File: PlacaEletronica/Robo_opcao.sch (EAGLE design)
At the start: 100 parts, among them IC1 7805DT, IC2 7805DT, J1 F-1X06-SIP-100-40, J2 S2B-PH-K-S(LF)(SN), J3 ZX62-B-5PA, Q1 SMD-TRANSISTORS-NPN-25V-500MW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, Q2 SMD-TRANSISTORS-NPN-25V-500MW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, Q4 SFH_3716, U1 ESP32-WROOM-32D, U2 AMS1117-3.3, U3 INTERFACE-CP2102-GMR(QFN28)QF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

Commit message: PlacaPrincipal_AlteracoesResistoresCapacitoresPinhead
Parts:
- C7: device rcl:C-EUC0402 -> Perfect_0402:CAP_0402
- R1, R44, R51, R52, R54, R55, R56, R57, R58: device resistors:R-EU_ -> Perfect_0402:RES_0402
- R53: device rcl:R-EU_R0603 -> Perfect_0402:RES_0402

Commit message: Biblioteca Waveform
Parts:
- removed U$2: TSOP4838, tsop-1:TSOP4838
- added Q5: TSOP4838, tsop:TSOP4838
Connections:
- net GND: now also Q5.GND; no longer U$2.GND
- net VDD33: now also Q5.V+; no longer U$2.V+
- net VP_SENSOR_IR: now also Q5.OUT; no longer U$2.OUT
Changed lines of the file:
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@@
 <setting verticaltext="up"/>
 </settings>
-<grid distance="50" unitdist="mil" unit="mil" style="lines" multiple="1" display="yes" altdistance="0.01" altunitdist="inch" altunit="inch"/>
+<grid distance="0.1" unitdist="inch" unit="inch" style="lines" multiple="1" display="no" altdistance="0.01" altunitdist="inch" altunit="inch"/>
 <layers>
 <layer number="1" name="Top" color="4" fill="1" visible="no" active="no"/>
@@
 <part name="C17" library="Perfect_0402" deviceset="CPOL_0402" device="" value="10uF"/>
 <part name="C18" library="Perfect_0402" deviceset="CPOL_0402" device="" value="20uF"/>
-<part name="U$2" library="tsop-1" deviceset="TSOP4838" device=""/>
+<part name="Q5" library="tsop" deviceset="TSOP4838" device=""/>
 </parts>
 <sheets>
@@
 <attribute name="VALUE" x="-164.211" y="203.454" size="1.778" layer="96" rot="R270"/>
 </instance>
-<instance part="U$2" gate="G$1" x="541.02" y="87.63" smashed="yes" rot="R270">
+<instance part="Q5" gate="G$1" x="541.02" y="87.63" smashed="yes" rot="R270">
 <attribute name="VALUE" x="549.402" y="93.472" size="1.778" layer="96" rot="R270"/>
 </instance>
@@
 <wire x1="535.94" y1="74.93" x2="532.13" y2="74.93" width="0.1524" layer="91"/>
 <label x="532.13" y="74.93" size="1.778" layer="95" rot="R180"/>
-<pinref part="U$2" gate="G$1" pin="GND"/>
+<pinref part="Q5" gate="G$1" pin="GND"/>
 <junction x="535.94" y="80.01"/>
 </segment>
@@
 <wire x1="546.1" y1="74.93" x2="549.91" y2="74.93" width="0.1524" layer="91"/>
 <label x="549.91" y="73.66" size="1.778" layer="95"/>
-<pinref part="U$2" gate="G$1" pin="V+"/>
+<pinref part="Q5" gate="G$1" pin="V+"/>
 <junction x="546.1" y="80.01"/>
 </segment>
@@
 <wire x1="541.02" y1="81.28" x2="541.02" y2="80.01" width="0.1524" layer="91"/>
 <label x="541.02" y="71.12" size="1.778" layer="95" rot="R180"/>
-<pinref part="U$2" gate="G$1" pin="OUT"/>
+<pinref part="Q5" gate="G$1" pin="OUT"/>
 <wire x1="541.02" y1="80.01" x2="541.02" y2="74.93" width="0.1524" layer="91"/>
 <junction x="541.02" y="80.01"/>

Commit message: [MODIFIED] Troca de pinagem na placa principal
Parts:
- removed J1: F-1X06-SIP-100-40, con-headers-jp(1):F-1X06-SIP-100-40
- removed JP10: F-1X10-SIP-100-40, con-headers-jp(1):F-1X10-SIP-100-40
- removed JP11, JP8: F-1X08-SIP-100-40, con-headers-jp(1):F-1X08-SIP-100-40
- removed JP2: F-1X05-SIP-100-40, con-headers-jp(1):F-1X05-SIP-100-40
- added J4: F-1X06-SIP-100-40, con-headers-jp(1):F-1X06-SIP-100-40
- added JP3, JP9: F-1X08-SIP-100-40, con-headers-jp(1):F-1X08-SIP-100-40
- added JP6: F-1X10-SIP-100-40, con-headers-jp(1):F-1X10-SIP-100-40
- added JP7: F-1X05-SIP-100-40, con-headers-jp(1):F-1X05-SIP-100-40
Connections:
- removed net 10(5V): U1.IO12, V3/2.B
- removed net 11(5V): U1.IO5, V3/3.B
- removed net 12(5V): U1.SHD/SD2, V3/4.B
- removed net 13(5V): U1.IO4, V4/1.B
- removed net 1_S: J1.1, U1.IO34
- removed net 2_S: J1.2, U1.IO35
- removed net 3_S: J1.3, U1.IO32
- removed net 4_S: J1.4, U1.IO33
- removed net 5_S: J1.5, U1.IO25
- removed net 6_S: J1.6, U1.IO26
- removed net 7_S: JP2.2, U1.IO27
- removed net 8_S: JP2.3, U1.IO15
- removed net 9(5V): U1.IO13, V3/1.B
- removed net N$29: JP8.1
- removed net N$48: JP10.8
- removed net PORT_10~5V: D11.A, JP2.5, U$12.D
- removed net PORT_11~5V: D12.A, JP11.3, U$13.D
- removed net PORT_12~5V: D13.A, JP11.8, U$14.D
- removed net PORT_13~5V: D14.A, JP11.7, U$15.D
- removed net PORT_9~5V: D10.A, JP2.4, U$11.D
- removed net PWM1(5V): U1.IO18, V4/2.B
- removed net PWM2(5V): U1.IO19, V4/3.B
- removed net PWM3(5V): U1.IO23, V4/4.B
- removed net PWM_1~5V: D15.A, JP11.4, U$16.D
- removed net PWM_2~5V: D16.A, JP11.5, U$17.D
- removed net PWM_3~5V: D17.A, JP11.6, U$18.D
- removed net SS: JP10.3, U1.IO2
- new net 5V(ATENçãO)-NãOESTACONECTADOEMNDA: JP9.5
- new net 5V(NAOTACONECTADOEMNDA): JP9.2
- new net IO12: J4.3, U1.IO12
- new net IO13: J4.4, U1.IO13
- new net IO15: U1.IO15, V4/2.B
- new net IO15-5V: D15.A, JP6.2, U$16.D
- new net IO18-SPI: JP6.6, U1.IO18
- new net IO19-SPI: JP6.5, U1.IO19
- new net IO2: J4.1, U1.IO2
- new net IO23-SPI: JP6.4, U1.IO23
- new net IO25: U1.IO25, V3/1.B
- new net IO25-5V: D10.A, JP3.3, U$11.D
- new net IO26: U1.IO26, V3/2.B
- new net IO26-5V: D11.A, JP3.4, U$12.D
- new net IO27: U1.IO27, V3/3.B
- new net IO27-5V: D12.A, JP3.5, U$13.D
- new net IO32: U1.IO32, V3/4.B
- new net IO32-5V: D13.A, JP3.6, U$14.D
- new net IO33: U1.IO33, V4/1.B
- new net IO33-5V: D14.A, JP3.7, U$15.D
- new net IO34: U1.IO34, V4/3.B
- new net IO34-5V: D16.A, JP3.8, U$17.D
- new net IO35: U1.IO35, V4/4.B
- new net IO35-5V: D17.A, JP6.1, U$18.D
- new net IO4: J4.2, U1.IO4
- new net IO5-SPI: JP6.3, U1.IO5
- new net RESET: JP6.8, JP9.3
- net 5V: no longer JP8.2, JP8.5
- net GND: now also JP6.7, JP9.6, JP9.7; no longer JP10.7, JP8.6, JP8.7
- net GND_PWM~5V: no longer JP2.1
- net I2C_SCL: now also JP6.10; no longer JP10.10
- net I2C_SDA: now also JP6.9; no longer JP10.9
- net MISO: no longer JP10.5
- net MOSI: no longer JP10.4
- net RX0: now also JP3.1; no longer JP11.1
- net SCK: no longer JP10.6
- net TX0: now also JP3.2; no longer JP11.2
- net VDD33: now also JP9.4; no longer JP8.4
- net VIN: now also JP9.8; no longer JP8.8
- net VN_SENSOR_IN: now also J4.6; no longer JP10.2
- net VP_SENSOR_IN: now also J4.5; no longer JP10.1

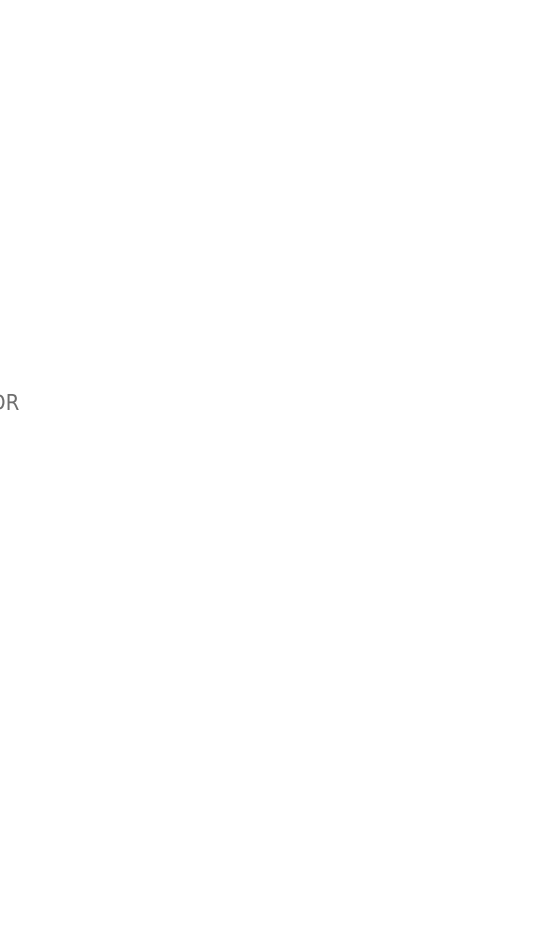
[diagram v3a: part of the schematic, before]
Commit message: [MODIFIED] Borda superior da placa, posicao e sentido pin heads
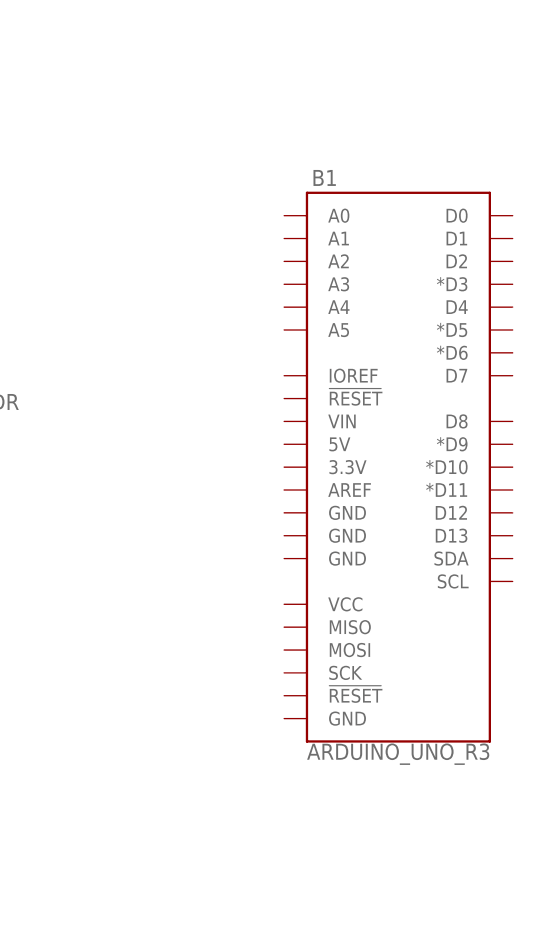
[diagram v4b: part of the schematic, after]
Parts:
- added B1: ARDUINO_UNO_R3, SparkFun-Boards:ARDUINO_UNO_R3
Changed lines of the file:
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@@
 <part name="JP7" library="con-headers-jp(1)" deviceset="F-1X05-" device="SIP-100-40"/>
 <part name="JP9" library="con-headers-jp(1)" library_urn="urn:adsk.eagle:library:24160814" deviceset="F-1X08-" device="SIP-100-40" package3d_urn="urn:adsk.eagle:package:24161226/2"/>
+<part name="B1" library="SparkFun-Boards" library_urn="urn:adsk.eagle:library:509" deviceset="ARDUINO_UNO_R3" device="" package3d_urn="urn:adsk.eagle:package:37330/1"/>
 </parts>
 <sheets>
@@
 <attribute name="VALUE" x="541.02" y="220.98" size="1.778" layer="96"/>
 </instance>
+<instance part="B1" gate="G$1" x="609.6" y="43.18" smashed="yes">
+<attribute name="NAME" x="599.948" y="74.422" size="1.778" layer="95" font="vector"/>
+<attribute name="VALUE" x="599.44" y="12.446" size="1.778" layer="96" font="vector" align="top-left"/>
+</instance>
 </instances>

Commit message: [Modified] Placa principal - Buzzer e conector alimentacao
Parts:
- removed J2: S2B-PH-K-S(LF)(SN), S2B-PH-K-S_LF__SN_:S2B-PH-K-S(LF)(SN)
- added J1: PJ-002A, PJ-002A:PJ-002A
- added LS2: PS1240P02BT, PS1240P02BT:PS1240P02BT
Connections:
- removed net 5V: JP4.4
- removed net 5V(ATENçãO)-NãOESTACONECTADOEMNDA: JP9.5
- removed net 5V(NAOTACONECTADOEMNDA): JP9.2
- removed net GND_PWM~5V: C34.2, C35.+, C36.2, C37.+, C38.2, C39.+, C40.2, C41.+, C5.2, C6.1, D10.C, D11.C, D12.C, D13.C, IC1.VO, U2.VIN, V3/+UB.+UB, V4/+UB.+UB
- new net GND_MOSFET: C34.2, C35.+, C36.2, C37.+, C38.2, C39.+, C40.2, C41.+, C5.2, C6.1, D10.C, D11.C, D12.C, D13.C, IC1.VO, JP4.4, JP9.2, JP9.5, U2.VIN, V3/+UB.+UB, V4/+UB.+UB
- net B+: now also J1.1; no longer J2.2
- net BUZZER: now also LS2.2
- net GND: now also J1.3, LS2.1; no longer J2.1
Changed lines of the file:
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@@
 <part name="R58" library="Perfect_0402" deviceset="RES_0402" device="" value="1R"/>
 <part name="J3" library="ZX62-B-5PA" deviceset="ZX62-B-5PA" device=""/>
-<part name="J2" library="S2B-PH-K-S_LF__SN_" deviceset="S2B-PH-K-S(LF)(SN)" device=""/>
 <part name="Q4" library="SFH_3716" deviceset="SFH_3716" device=""/>
 <part name="R6" library="rcl" library_urn="urn:adsk.eagle:library:334" deviceset="R-EU_" device="M0805" package3d_urn="urn:adsk.eagle:package:23556/2" value="1k"/>
@@
 <part name="JP9" library="con-headers-jp(1)" library_urn="urn:adsk.eagle:library:24160814" deviceset="F-1X08-" device="SIP-100-40" package3d_urn="urn:adsk.eagle:package:24161226/2"/>
 <part name="B1" library="SparkFun-Boards" library_urn="urn:adsk.eagle:library:509" deviceset="ARDUINO_UNO_R3" device="" package3d_urn="urn:adsk.eagle:package:37330/1"/>
+<part name="J1" library="PJ-002A" deviceset="PJ-002A" device=""/>
+<part name="LS2" library="PS1240P02BT" deviceset="PS1240P02BT" device=""/>
 </parts>
 <sheets>
@@
 <attribute name="NAME" x="-50.8107" y="10.9362" size="1.77986875" layer="95"/>
 </instance>
-<instance part="J2" gate="G$1" x="38.1" y="68.58" smashed="yes" rot="R90">
-<attribute name="NAME" x="34.798" y="63.5" size="1.778" layer="95" rot="R90"/>
-<attribute name="VALUE" x="45.72" y="63.5" size="1.778" layer="96" rot="R90"/>
-</instance>
 <instance part="Q4" gate="G$1" x="543.56" y="114.3" smashed="yes" rot="R90">
 <attribute name="VALUE" x="551.18" y="104.14" size="1.778" layer="96" rot="R90"/>
@@
 <attribute name="NAME" x="599.948" y="74.422" size="1.778" layer="95" font="vector"/>
 <attribute name="VALUE" x="599.44" y="12.446" size="1.778" layer="96" font="vector" align="top-left"/>
+</instance>
+<instance part="J1" gate="G$1" x="40.64" y="64.77" smashed="yes" rot="R270">
+<attribute name="NAME" x="45.720790625" y="72.39118125" size="1.77828125" layer="95" rot="R270"/>
+<attribute name="VALUE" x="35.55176875" y="72.40235" size="1.78088125" layer="96" rot="R270"/>
+</instance>
+<instance part="LS2" gate="G$1" x="180.34" y="139.7" smashed="yes" rot="R90">
+<attribute name="NAME" x="176.53" y="135.89" size="1.778" layer="95" rot="R90"/>
+<attribute name="VALUE" x="185.42" y="135.89" size="1.778" layer="96" rot="R90"/>
 </instance>
 </instances>
@@
 <segment>
 <label x="38.1" y="53.34" size="1.27" layer="95" rot="R270" xref="yes"/>
-<pinref part="J2" gate="G$1" pin="1"/>
-<wire x1="38.1" y1="58.42" x2="38.1" y2="53.34" width="0.1524" layer="91"/>
+<pinref part="J1" gate="G$1" pin="3"/>
+<wire x1="38.1" y1="55.88" x2="38.1" y2="53.34" width="0.1524" layer="91"/>
+<wire x1="38.1" y1="55.88" x2="40.64" y2="55.88" width="0.1524" layer="91"/>
+<wire x1="40.64" y1="55.88" x2="40.64" y2="59.69" width="0.1524" layer="91"/>
 </segment>
 <segment>
@@
 <label x="552.45" y="231.14" size="1.778" layer="95" rot="R180"/>
 </segment>
+<segment>
+<pinref part="LS2" gate="G$1" pin="1"/>
+<wire x1="180.34" y1="134.62" x2="180.34" y2="132.08" width="0.1524" layer="91"/>
+<label x="180.34" y="132.08" size="1.778" layer="95"/>
+</segment>
 </net>
 <net name="SCREEN_RX" class="0">
@@
 <wire x1="553.72" y1="224.79" x2="552.45" y2="224.79" width="0.1524" layer="91"/>
 <label x="552.45" y="226.06" size="1.778" layer="95" rot="R180"/>
-</segment>
-</net>
-<net name="5V" class="0">
-<segment>
-<pinref part="JP4" gate="A" pin="4"/>
-<wire x1="527.05" y1="-43.18" x2="535.94" y2="-43.18" width="0.1524" layer="91"/>
-<label x="535.94" y="-43.18" size="1.778" layer="95"/>
 </segment>
 </net>
@@
 <label x="180.34" y="175.26" size="1.778" layer="95"/>
 </segment>
+<segment>
+<pinref part="LS2" gate="G$1" pin="2"/>
+<wire x1="180.34" y1="144.78" x2="180.34" y2="147.32" width="0.1524" layer="91"/>
+<label x="180.34" y="147.32" size="1.778" layer="95" rot="R180"/>
+</segment>
 </net>
 <net name="EN" class="0">
@@
 <wire x1="43.18" y1="55.88" x2="43.18" y2="53.34" width="0.1524" layer="91"/>
 <label x="43.18" y="53.34" size="1.27" layer="95" rot="R270" xref="yes"/>
-<pinref part="J2" gate="G$1" pin="2"/>
-<wire x1="40.64" y1="58.42" x2="43.18" y2="58.42" width="0.1524" layer="91"/>
-<wire x1="43.18" y1="58.42" x2="43.18" y2="55.88" width="0.1524" layer="91"/>
+<wire x1="43.18" y1="59.69" x2="43.18" y2="55.88" width="0.1524" layer="91"/>
 <junction x="43.18" y="55.88"/>
+<pinref part="J1" gate="G$1" pin="1"/>
 </segment>
 <segment>
@@
 </segment>
 </net>
-<net name="GND_PWM~5V" class="0">
+<net name="GND_MOSFET" class="0">
 <segment>
 <pinref part="V3" gate="/+UB" pin="+UB"/>
@@
 <junction x="327.66" y="31.75"/>
 </segment>
+<segment>
+<pinref part="JP9" gate="G$1" pin="2"/>
+<wire x1="553.72" y1="240.03" x2="552.45" y2="240.03" width="0.1524" layer="91"/>
+<label x="552.45" y="241.3" size="1.778" layer="95" rot="R180"/>
+</segment>
+<segment>
+<pinref part="JP9" gate="G$1" pin="5"/>
+<wire x1="553.72" y1="232.41" x2="552.45" y2="232.41" width="0.1524" layer="91"/>
+<label x="552.45" y="233.68" size="1.778" layer="95" rot="R180"/>
+</segment>
+<segment>
+<pinref part="JP4" gate="A" pin="4"/>
+<wire x1="527.05" y1="-43.18" x2="535.94" y2="-43.18" width="0.1524" layer="91"/>
+<label x="535.94" y="-43.18" size="1.778" layer="95"/>
+</segment>
 </net>
 <net name="N$28" class="0">
@@
 </segment>
 </net>
-<net name="5V(ATENçãO)-NãOESTACONECTADOEMNDA" class="0">
-<segment>
-<pinref part="JP9" gate="G$1" pin="5"/>
-<wire x1="553.72" y1="232.41" x2="552.45" y2="232.41" width="0.1524" layer="91"/>
-<label x="552.45" y="233.68" size="1.778" layer="95" rot="R180"/>
-</segment>
-</net>
-<net name="5V(NAOTACONECTADOEMNDA)" class="0">
-<segment>
-<pinref part="JP9" gate="G$1" pin="2"/>
-<wire x1="553.72" y1="240.03" x2="552.45" y2="240.03" width="0.1524" layer="91"/>
-<label x="552.45" y="241.3" size="1.778" layer="95" rot="R180"/>
-</segment>
-</net>
